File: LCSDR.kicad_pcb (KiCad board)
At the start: 2 copper layers, 150 x 95 mm, 134 parts, among them J1 Conn_01x10, J10 Conn_01x01, J11 Conn_01x01, J2 Conn_01x10, J3 phones, J4 MIC_PTT, J5 Conn_01x10, J8 Conn_01x01, J9 Conn_01x01, K2 G6K-2F, K3 G6K-2F, Q1 MMBT2222LT1G, Q2 BC847, U1 4053, U10 NE5532, U11 MC33079, U2 74LVC1G74, U3 4053, U4 74LVC1G74, U5 FSA3157, U6 NE5532, U7 FSA3157

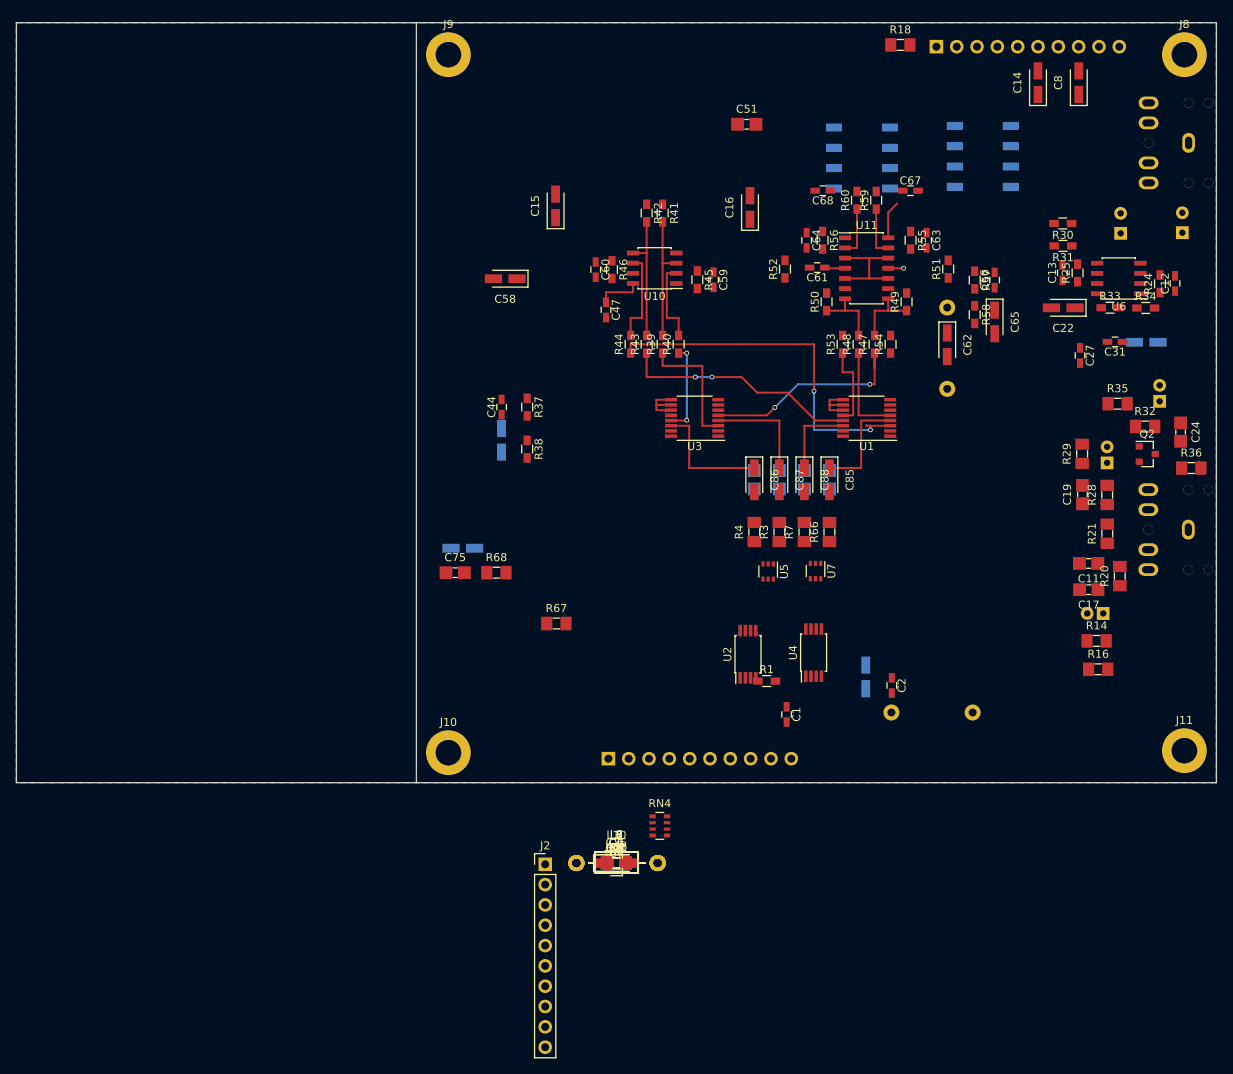
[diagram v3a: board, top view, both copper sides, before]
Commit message: need some GND vias
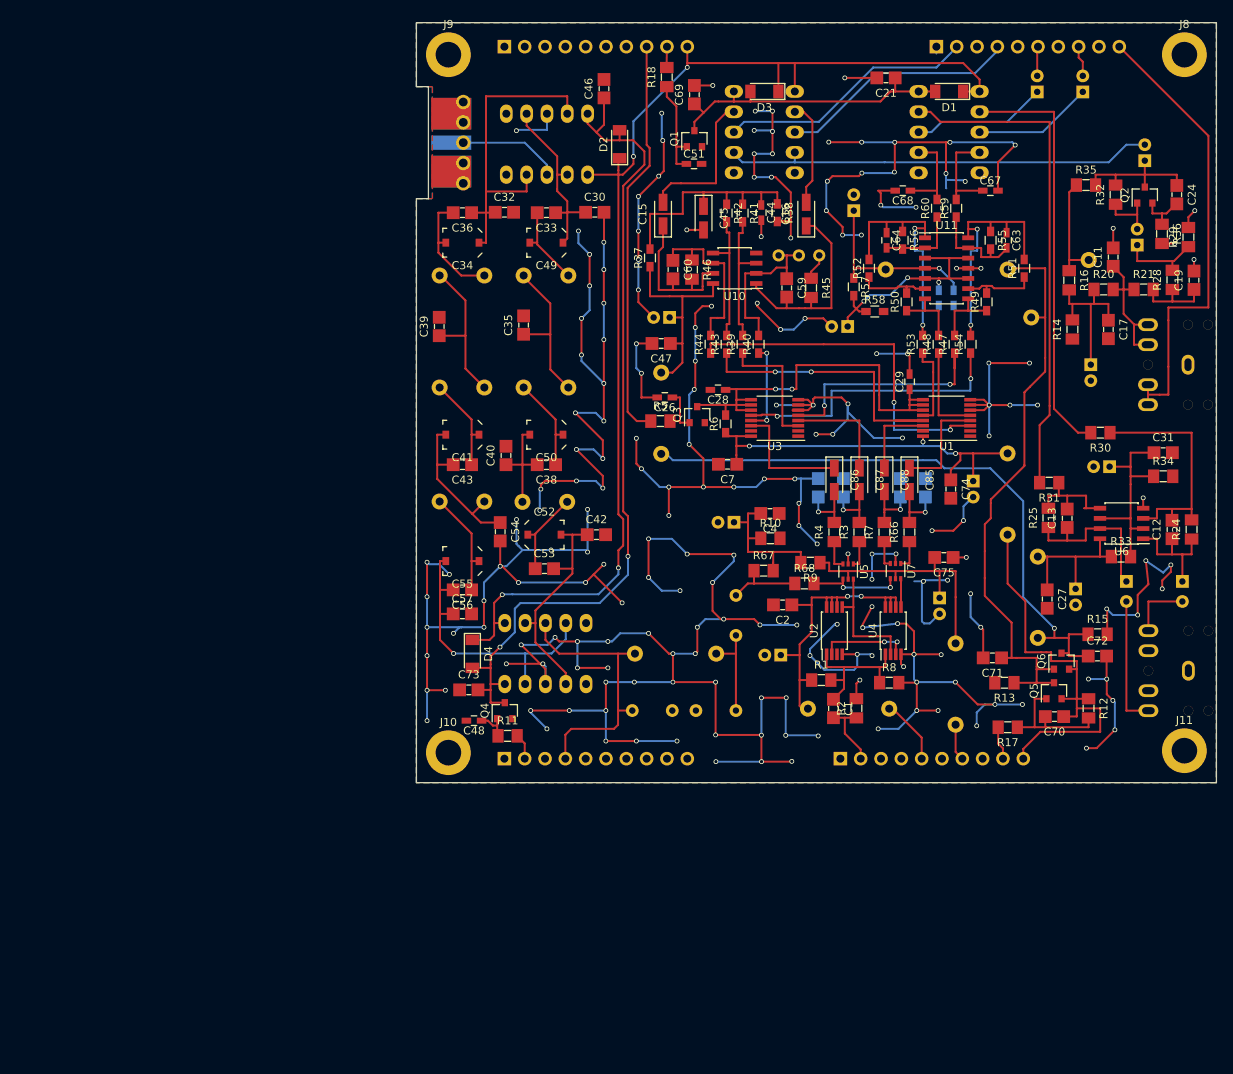
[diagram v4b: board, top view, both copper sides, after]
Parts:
- removed RN4: 47, Resistors_SMD:R_Array_Convex_4x0603
- added C26: 10...22nF, Capacitors_SMD:C_0603_HandSoldering, F.Cu at (146.1, 86.8)
- added C28: 10...22nF, Capacitors_SMD:C_0603_HandSoldering, F.Cu at (152.7, 85.9)
- added C29: 10...22nF, Capacitors_SMD:C_0603_HandSoldering, F.Cu at (176.7, 84.9)
- added C30: C_Small, UI:C_1206_0603, F.Cu at (137.3, 63.7)
- added C32: C_Small, UI:C_1206_0603, F.Cu at (126.0, 63.7)
- added C33: C_Small, UI:C_1206_0603, F.Cu at (131.2, 63.8)
- added C34: C_Variable, Capacitors_SMD:C_Trimmer_Murata_TZC3, F.Cu at (120.8, 67.5)
- added C35: C_Small, UI:C_1206_0603, F.Cu at (128.4, 77.8)
- added C36: C_Small, UI:C_1206_0603, F.Cu at (120.8, 63.8)
- added C38: C_Small, UI:C_1206_0603, F.Cu at (131.2, 95.2)
- added C39: C_Small, UI:C_1206_0603, F.Cu at (117.9, 78.0)
- added C40: C_Small, UI:C_1206_0603, F.Cu at (126.2, 94.1)
- added C41: C_Variable, Capacitors_SMD:C_Trimmer_Murata_TZC3, F.Cu at (120.8, 91.5)
- added C42: C_Small, UI:C_1206_0603, F.Cu at (137.5, 104.0)
- added C43: C_Small, UI:C_1206_0603, F.Cu at (120.8, 95.2)
- added C46: 100nF, UI:C_1206_0603, F.Cu at (138.4, 48.2)
- added C48: 15nF, Capacitors_SMD:C_0603_HandSoldering, F.Cu at (122.2, 127.2)
- added C49: C_Variable, Capacitors_SMD:C_Trimmer_Murata_TZC3, F.Cu at (131.2, 67.5)
- added C50: C_Variable, Capacitors_SMD:C_Trimmer_Murata_TZC3, F.Cu at (131.2, 91.5)
- added C52: C_Variable, Capacitors_SMD:C_Trimmer_Murata_TZC3, F.Cu at (131.0, 104.0)
- added C53: C_Small, UI:C_1206_0603, F.Cu at (131.0, 108.2)
- added C54: C_Small, UI:C_1206_0603, F.Cu at (125.5, 103.6)
- added C55: C_Variable, Capacitors_SMD:C_Trimmer_Murata_TZC3, F.Cu at (120.8, 107.3)
- added C56: C_Small, UI:C_1206_0603, F.Cu at (120.8, 110.9)
- added C57: C_Small, UI:C_1206_0603, F.Cu at (120.8, 113.9)
- added C69: 100nF, UI:C_1206_0603, F.Cu at (149.8, 49.0)
- added C70: 100nF, UI:C_1206_0603, F.Cu at (194.8, 126.7)
- added C71: 100nF, UI:C_1206_0603, F.Cu at (187.0, 119.4)
- added C72: 100nF, UI:C_1206_0603, F.Cu at (200.1, 119.2)
- added C73: 100nF, UI:C_1206_0603, F.Cu at (121.5, 123.4)
- added C74: 100nF, UI:C_1206_0603, F.Cu at (181.8, 98.3)
- added C77: 100nF, Capacitors_THT:C_Disc_D7.0mm_W2.5mm_P5.00mm, B.Cu at (142.0, 126.0)
- added C78: 100nF, Capacitors_THT:C_Disc_D7.0mm_W2.5mm_P5.00mm, B.Cu at (154.9, 126.0)
- added D1: LL4148, Diodes_SMD:D_MiniMELF, F.Cu at (181.6, 48.6)
- added D2: LL4148, Diodes_SMD:D_MiniMELF, F.Cu at (140.4, 55.2)
- added D3: LL4148, Diodes_SMD:D_MiniMELF, F.Cu at (158.5, 48.6)
- added D4: LL4148, Diodes_SMD:D_MiniMELF, F.Cu at (122.0, 118.9)
- added J6: Conn_Coaxial, UI:RFCONNECTOR, B.Cu at (122.0, 55.0)
- added J7: Conn_01x10, Pin_Headers:Pin_Header_Straight_1x10_Pitch2.54mm, B.Cu at (126.0, 43.0)
- added K1: FRT5, Relays_THT:Relay_DPDT_FRT5, B.Cu at (136.4, 59.0)
- added K4: FRT5, Relays_THT:Relay_DPDT_FRT5, B.Cu at (126.0, 115.0)
- added L11: L_Small, Choke_Toroid_ThroughHole:Choke_Toroid_6,5x13mm_Vertical, B.Cu at (124.0, 79.0)
- added L12: L_Small, Choke_Toroid_ThroughHole:Choke_Toroid_6,5x13mm_Vertical, B.Cu at (127.8, 106.5)
- added L13: L_Small, Choke_Toroid_ThroughHole:Choke_Toroid_6,5x13mm_Vertical, B.Cu at (124.0, 93.2)
- added L14: 33uH, Choke_Axial_ThroughHole:Choke_Horizontal_RM10mm, B.Cu at (147.3, 118.9)
- added L3: L_Small, Choke_Toroid_ThroughHole:Choke_Toroid_6,5x13mm_Vertical, B.Cu at (134.5, 65.0)
- added L4: L_Small, Choke_Toroid_ThroughHole:Choke_Toroid_6,5x13mm_Vertical, B.Cu at (124.0, 65.0)
- added L9: L_Small, Choke_Toroid_ThroughHole:Choke_Toroid_6,5x13mm_Vertical, B.Cu at (134.5, 79.0)
- added Q3: MMBT2222LT1G, TO_SOT_Packages_SMD:SOT-23, F.Cu at (150.1, 89.0)
- added Q4: MMBT2222LT1G, TO_SOT_Packages_SMD:SOT-23, F.Cu at (126.0, 126.0)
- added Q5: Si2301, TO_SOT_Packages_SMD:SOT-23, F.Cu at (194.7, 123.5)
- added Q6: Si2301, TO_SOT_Packages_SMD:SOT-23, F.Cu at (195.6, 119.8)
- added R11: 2.2k, UI:R_1206_0603, F.Cu at (126.4, 129.2)
- added R12: 2.2k, UI:R_1206_0603, F.Cu at (199.0, 125.7)
- added R13: 4.7k, UI:R_1206_0603, F.Cu at (188.5, 122.5)
- added R15: 4.7k, UI:R_1206_0603, F.Cu at (200.2, 116.5)
- added R17: 2.2k, UI:R_1206_0603, F.Cu at (188.9, 128.1)
- added R5: 2.2k, UI:R_1206_0603, F.Cu at (145.5, 89.8)
- added R6: 10k, Resistors_SMD:R_0603_HandSoldering, F.Cu at (153.7, 90.2)
- added RV1: 5k, UI:Potentiometer_Bourns_3296W_3-8Zoll_Inline_ScrewUp, B.Cu at (165.4, 69.1)
- C1, C2, C27, C31, C47, C59, C60, C7: footprint Capacitors_SMD:C_0603_HandSoldering -> UI:C_1206_0603
- C11: value 3.3nF -> 1.5nF
- C12, C13: value 100nF -> 220pF; footprint Capacitors_SMD:C_0603_HandSoldering -> UI:C_1206_0603
- C14, C22, C25, C58, C6, C62, C65, C8: footprint Capacitors_Tantalum_SMD:CP_Tantalum_Case-A_EIA-3216-18_Wave -> Capacitors_THT:CP_Radial_D5.0mm_P2.00mm; moved to B.Cu
- C23, C3, C76: footprint Capacitors_Tantalum_SMD:CP_Tantalum_Case-A_EIA-3216-18_Wave -> Capacitors_THT:CP_Radial_D5.0mm_P2.00mm
- C45: moved to F.Cu
- C5: footprint UI:C_1206_0603 -> Capacitors_THT:C_Disc_D7.0mm_W2.5mm_P5.00mm; moved to B.Cu
- C51: footprint UI:C_1206_0603 -> Capacitors_SMD:C_0603_HandSoldering
- C61, C66, L10, L2, L5, L6, L7: moved to B.Cu
- J1: renamed from J2; moved to B.Cu
- K2, K3: value G6K-2F -> FRT5; footprint UI:Relay_G6K-2F -> Relays_THT:Relay_DPDT_FRT5
- L8: footprint Choke_Axial_ThroughHole:Choke_Horizontal_RM10mm -> Choke_Axial_ThroughHole:Choke_Horizontal_RM15mm
- R1, R2, R24, R25, R33, R34, R46, R8: footprint Resistors_SMD:R_0603_HandSoldering -> UI:R_1206_0603
- R30, R31: value 10k -> 6.8k; footprint Resistors_SMD:R_0603_HandSoldering -> UI:R_1206_0603
- R45: value 22k -> 20k; footprint Resistors_SMD:R_0603_HandSoldering -> UI:R_1206_0603
- moved C21 103.8 mm to (173.7, 46.9), turned to 180 degrees
- moved Q1 91.1 mm to (149.8, 54.5), turned to 90 degrees
- moved L6 90.8 mm to (195.5, 73.2), turned to 225 degrees
- moved L2 67.2 mm to (188.9, 99.0), turned to 90 degrees
- moved J3 66.0 mm to (211.5, 121.0)
- moved C25 65.3 mm to (184.6, 97.3), turned to 270 degrees
- moved L5 62.2 mm to (192.7, 111.9), turned to 90 degrees
- moved C75 61.1 mm to (180.9, 106.8), turned to 180 degrees
- moved C76 59.9 mm to (180.4, 111.9), turned to 270 degrees
- moved L7 56.4 mm to (145.6, 88.9), turned to 90 degrees
- moved C7 51.8 mm to (153.9, 95.2), turned to 180 degrees
- moved R16 48.8 mm to (196.6, 72.2), turned to 270 degrees
- moved L10 47.9 mm to (182.4, 122.8), turned to 90 degrees
- moved C4 47.7 mm to (159.2, 101.3), turned to 180 degrees
- moved C6 45.1 mm to (154.7, 102.5), turned to 180 degrees
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- renumbered J1 to J2
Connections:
- C14 pad 2: LINE_OUT_LEFT -> LINE_OUT_RIGHT
- C5 pad 1: (no net) -> Net-(C5-Pad1)
- C8 pad 2: LINE_OUT_RIGHT -> LINE_OUT_LEFT
- J1 pad 1: Voltage1 -> GND
- J1 pad 2: (no net) -> BAND
- J1 pad 3: (no net) -> GND
- J1 pad 4: (no net) -> BPF
- J1 pad 5: (no net) -> GND
- J1 pad 6: Net-(J2-Pad6) -> (no net)
- J1 pad 7: Net-(J2-Pad7) -> (no net)
- J1 pad 8: Net-(J2-Pad8) -> (no net)
- J1 pad 9: Net-(J2-Pad9) -> (no net)
- J2 pad 10: (no net) -> +9V
- J2 pad 4: (no net) -> GND
- J2 pad 5: GND -> ROTATE
- J2 pad 6: (no net) -> GND
- J2 pad 7: GND -> MIXER
- J2 pad 8: (no net) -> GND
- J2 pad 9: (no net) -> IF_RX_TX
- J4 pad 1: (no net) -> PTT
- J4 pad 4: (no net) -> PTT
- J5 pad 10: (no net) -> PTT
- K2 pad 1: (no net) -> +12V
- K2 pad 10: (no net) -> Net-(C21-Pad1)
- K2 pad 3: LINE_IN_LEFT -> LINE_IN_RIGHT
- K2 pad 8: LINE_IN_RIGHT -> LINE_IN_LEFT
- K3 pad 1: (no net) -> +12V
- L1 pad 1: Voltage1 -> ROTATE
- L10 pad 1: Voltage1 -> MIXER
- L2 pad 1: (no net) -> +9V
- L5 pad 1: TX_9V -> RX_9V
- L7 pad 1: (no net) -> RX_9V
- R18 pad 2: (no net) -> S2_RX_TX
- R45 pad 1: Net-(C59-Pad1) -> Net-(R45-Pad1)
- U2 pad 3: Net-(U2-Pad3) -> (no net)
- U2 pad 5: P90 -> P0
- U4 pad 2: Net-(U2-Pad3) -> P0
- U4 pad 3: P0 -> Net-(U2-Pad2)
- U4 pad 5: Net-(U2-Pad2) -> P90
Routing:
- net GND: track 1.93 -> 812.1 mm, vias 1 -> 197
- net +12V: track 0.00 -> 150.4 mm, vias 0 -> 4
- net Net-(C46-Pad1): track 0.00 -> 106.8 mm, vias 0 -> 2
- net RX_9V: track 0.00 -> 79.4 mm, vias 0 -> 1
- net TX_9V: track 0.00 -> 74.4 mm
- net Net-(K3-Pad9): track 0.00 -> 62.5 mm
- net PTT: track 0.00 -> 58.2 mm
- net Net-(C37-Pad2): track 0.00 -> 54.1 mm
- net +9V: track 0.00 -> 53.6 mm
- net Net-(K3-Pad2): track 0.00 -> 52.3 mm
- net Net-(C32-Pad1): track 0.00 -> 51.8 mm
- net S1_RX_TX: track 0.00 -> 50.3 mm
- net VDD: track 0.00 -> 49.7 mm, vias 0 -> 3
- net Net-(C28-Pad1): track 13.1 -> 53.9 mm, vias 0 -> 2
- net VCC: track 0.00 -> 39.5 mm, vias 0 -> 2
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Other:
- board size 150 x 95 mm -> 100 x 95 mm

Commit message: production
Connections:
- J6 pad 1: Net-(J6-Pad1) -> OUT
- J7 pad 1: (no net) -> GND
- J7 pad 2: (no net) -> OUT
- J7 pad 3: (no net) -> GND
- K1 pad 3: Net-(J6-Pad1) -> OUT
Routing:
- net GND: track 812.1 -> 1018.7 mm, vias 197 -> 236
- net OUT: track 0.00 -> 27.9 mm
- net Net-(J6-Pad1): track 14.3 -> 0.00 mm

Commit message: Phase shift with 74LCX574 TSSOP-20
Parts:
- removed C1: 1.5nF, UI:C_1206_0603
- removed R1, R2, R8: 1k, UI:R_1206_0603
- added C79: 100nF, UI:C_1206_0603, F.Cu at (163.0, 124.9)
- added U8: 74LCX574, Housings_SSOP:TSSOP-20_4.4x6.5mm_Pitch0.65mm, F.Cu at (172.0, 116.9)
- U2, U4: value 74LVC1G74 -> 74LVC1G00DCKR; footprint Housings_SSOP:TSSOP-8_4.4x3mm_Pitch0.65mm -> TO_SOT_Packages_SMD:SOT-353_SC-70-5
- U5, U7: footprint TO_SOT_Packages_SMD:SOT-363_SC-70-6 -> TO_SOT_Packages_SMD:SOT-23-6
- moved U4 9.11 mm to (175.7, 125.0)
- moved U2 7.31 mm to (169.2, 123.0), turned to 180 degrees
- moved L1 5.05 mm to (173.2, 128.7)
- moved C2 4.76 mm to (165.4, 114.0)
- moved C3 2.20 mm to (161.0, 116.9)
- moved L10 1.96 mm to (183.4, 121.1)
- moved R68 1.21 mm to (162.4, 110.6)
- moved R9 1.10 mm to (163.2, 107.5)
- moved R67 0.73 mm to (157.7, 108.7), turned to 90 degrees
- moved U5 0.23 mm to (168.8, 108.5)
- moved U7 0.16 mm to (175.1, 108.5)
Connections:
- U2 pad 1: Net-(C1-Pad1) -> Net-(U2-Pad1)
- U2 pad 2: Net-(U2-Pad2) -> Net-(U2-Pad1)
- U2 pad 3: (no net) -> GND
- U2 pad 4: GND -> Net-(U2-Pad4)
- U2 pad 5: P0 -> VCC
- U4 pad 1: Net-(C1-Pad1) -> CLK
- U4 pad 2: P0 -> CLK
- U4 pad 3: Net-(U2-Pad2) -> GND
- U4 pad 4: GND -> Net-(U4-Pad4)
- U4 pad 5: P90 -> VCC
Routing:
- net GND: track 1018.7 -> 1039.3 mm, vias 236 -> 237
- net Net-(C1-Pad1): track 18.7 -> 0.00 mm
- net P90: track 3.61 -> 15.8 mm
- net Net-(U2-Pad1): track 0.00 -> 12.2 mm
- net Net-(U2-Pad2): track 11.3 -> 0.00 mm, vias 2 -> 0
- net Net-(U4-Pad4): track 0.00 -> 10.7 mm
- net Net-(U2-Pad4): track 0.00 -> 9.62 mm
- net Net-(U8-Pad19): track 0.00 -> 6.55 mm
- net ROTATE: track 8.19 -> 3.32 mm
- net VCC: track 39.5 -> 36.8 mm, vias 2 -> 0
- net P0: track 15.4 -> 13.1 mm, vias 0 -> 2
- net Net-(C4-Pad2): track 20.1 -> 18.0 mm
- net MIXER: track 4.60 -> 5.99 mm
- net Net-(C5-Pad2): track 9.58 -> 8.35 mm
- net CLK: track 8.82 -> 9.59 mm
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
